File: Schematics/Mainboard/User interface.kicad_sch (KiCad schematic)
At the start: 42 parts, among them J16 OLED, J18 Power, J19 Power, J20 I0, J21 Data, J22 Data, J23 I1, J24 I2C OLED 0, J25 I2C OLED 1, J26 I2C OLED 2, J27 I2C OLED 3, J28 I2C OLED 4, J29 I2C OLED 5, J30 I2C OLED 6, J31 I2C OLED 7, J32 I2, J33 I3, J34 O0, J35 O1, J36 O2, J37 O3, J9 ICSP, U2 TCA9548APWR, U3 ATmega328-AU, Y1 16MHz YSX321SL

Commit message: Added Mainboard rev 1.0
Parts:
- removed C5, C6: 0u1, Capacitor_SMD:C_0603_1608Metric, symbol Device:C_Small
- removed J18, J19: Power, Connector_PinSocket_2.54mm:PinSocket_1x03_P2.54mm_Vertical, symbol Connector:Conn_01x03_Male
- removed J21, J22: Data, Connector_PinSocket_2.54mm:PinSocket_1x03_P2.54mm_Vertical, symbol Connector:Conn_01x03_Male
- removed J9: ICSP, Connector_PinSocket_2.54mm:PinSocket_2x03_P2.54mm_Vertical, symbol Connector_Generic:Conn_02x03_Odd_Even
- removed U3: ATmega328-AU, Package_QFP:TQFP-32_7x7mm_P0.8mm, symbol MCU_Microchip_ATmega:ATmega328-AU
- removed Y1: 16MHz YSX321SL, Crystal:Crystal_SMD_3225-4Pin_3.2x2.5mm, symbol Device:Crystal_GND24_Small
- added J44: Del in, custom:PinSocket_1x06_P2.54mm_Vertical, symbol Connector:Conn_01x06_Male
- added J45: Del out, custom:PinSocket_1x06_P2.54mm_Vertical, symbol Connector:Conn_01x06_Male
- added JP3, JP4: Jumper, Jumper:SolderJumper-2_P1.3mm_Open_Pad1.0x1.5mm, symbol Device:Jumper
- added R17, R18, R19: 47k, Resistor_SMD:R_0603_1608Metric, symbol Device:R_Small
- added SW3, SW4: Rot, Rotary_Encoder:RotaryEncoder_Alps_EC11E-Switch_Vertical_H20mm, symbol Device:Rotary_Encoder_Switch
- added U4: PCF8574TS, Package_SO:SSOP-20_4.4x6.5mm_P0.65mm, symbol Interface_Expansion:PCF8574TS
- C4: LCSC Part (none) -> C19702
- C7, C8: value 12p -> 10u; LCSC Part (none) -> C19702
- D4: footprint LED_SMD:LED_SK6805_PLCC4_2.4x2.7mm_P1.3mm -> LED_THT:LED_BL-FL7680RGB; symbol Device:LED_ABGR -> Device:LED_BRGA
- J16, J24, J25, J26, J27, J28, J29, J30, J31: footprint Connector_PinHeader_2.54mm:PinHeader_1x04_P2.54mm_Vertical_SMD_Pin1Left -> Connector_PinSocket_2.54mm:PinSocket_1x04_P2.54mm_Vertical
- R11, R13: value 1K -> 47k; LCSC Part (none) -> C25819
- R12, R14, R15: value 10K -> 10k; LCSC Part (none) -> C25804
- R16: value 10K -> 47k; LCSC Part (none) -> C25819
- R9: LCSC Part (none) -> C22810
- U2: LCSC Part (none) -> C130026
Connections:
- net 3.3V_local is gone; now on an unnamed net: D4.1 (BK)
- net ICSP RST is gone; now on net T A: R16.1
- net SUB RX is gone; now on net +3V3: R11.2
- net SUB TX is gone; now on net +3V3: R13.2
- net XTAL1 is gone; now on net GND: C7.2
- net XTAL2 is gone; now on net +3V3: C8.1
- net +3V3: now also C7.1, D4.4 (A), J44.2 (Pin_2), R17.2, R18.2, R19.2, U4.5 (VDD)
- net ALT SCL: now also U4.2 (SCL)
- net ALT SDA: now also U4.4 (SDA)
- net GND: now also J44.5 (Pin_5), SW3.C, SW3.S2, SW4.C, SW4.S2, U4.15 (VSS), U4.6 (A0), U4.7 (A1), U4.9 (A2); no longer C7.1
- net MUX SCL: now also J44.4 (Pin_4), JP4.1; no longer R12.1, U2.22 (SCL)
- net MUX SDA: now also J44.3 (Pin_3), JP3.1; no longer R14.1, U2.23 (SDA)
- net Q A: now also R17.1, SW4.A
- net Q B: now also R13.1, SW4.B
- net Q SW: now also R19.1, SW4.S1
- net T A: now also SW3.A
- net T B: now also R11.1, SW3.B
- net T SW: now also R18.1, SW3.S1
- net at J36.1 (Pin_1): now also U4.19 (P6)
- net at J33.1 (Pin_1): now also U4.16 (P4)
- net at J23.1 (Pin_1): now also U4.12 (P2)
- net at R8.1: no longer D4.2 (BK)
- net at J37.1 (Pin_1): now also U4.20 (P7)
- net at J32.1 (Pin_1): now also U4.14 (P3)
- net at J34.1 (Pin_1): now also U4.10 (P0)
- net at J35.1 (Pin_1): now also U4.17 (P5)
- net at R10.1: now also D4.2 (RK); no longer D4.4 (RK)
- net at J20.1 (Pin_1): now also U4.11 (P1)
- new net Expand INT: U4.1 (~INT~)
- new net OLED SCL: J45.4 (Pin_4), JP4.2, R12.1, U2.22 (SCL)
- new net OLED SDA: J45.3 (Pin_3), JP3.2, R14.1, U2.23 (SDA)
- no-connect marks 3 -> 6
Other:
- note added: "I/O expander"
- note added: "OLED Deligate"
- note added: "OLED Deligate module"
- note added: "Rotary encoders"
- note removed: "CL = (C1 * C2) / (C1 + C2) + Cstray 9pF = (12pF^2)/(12pF*2) + 3pF"
- note removed: "Rot enc module"
- moved on the sheet: D4, J16, J20, J23, J32, J33, J34, J35, J36, J37, R10, R8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

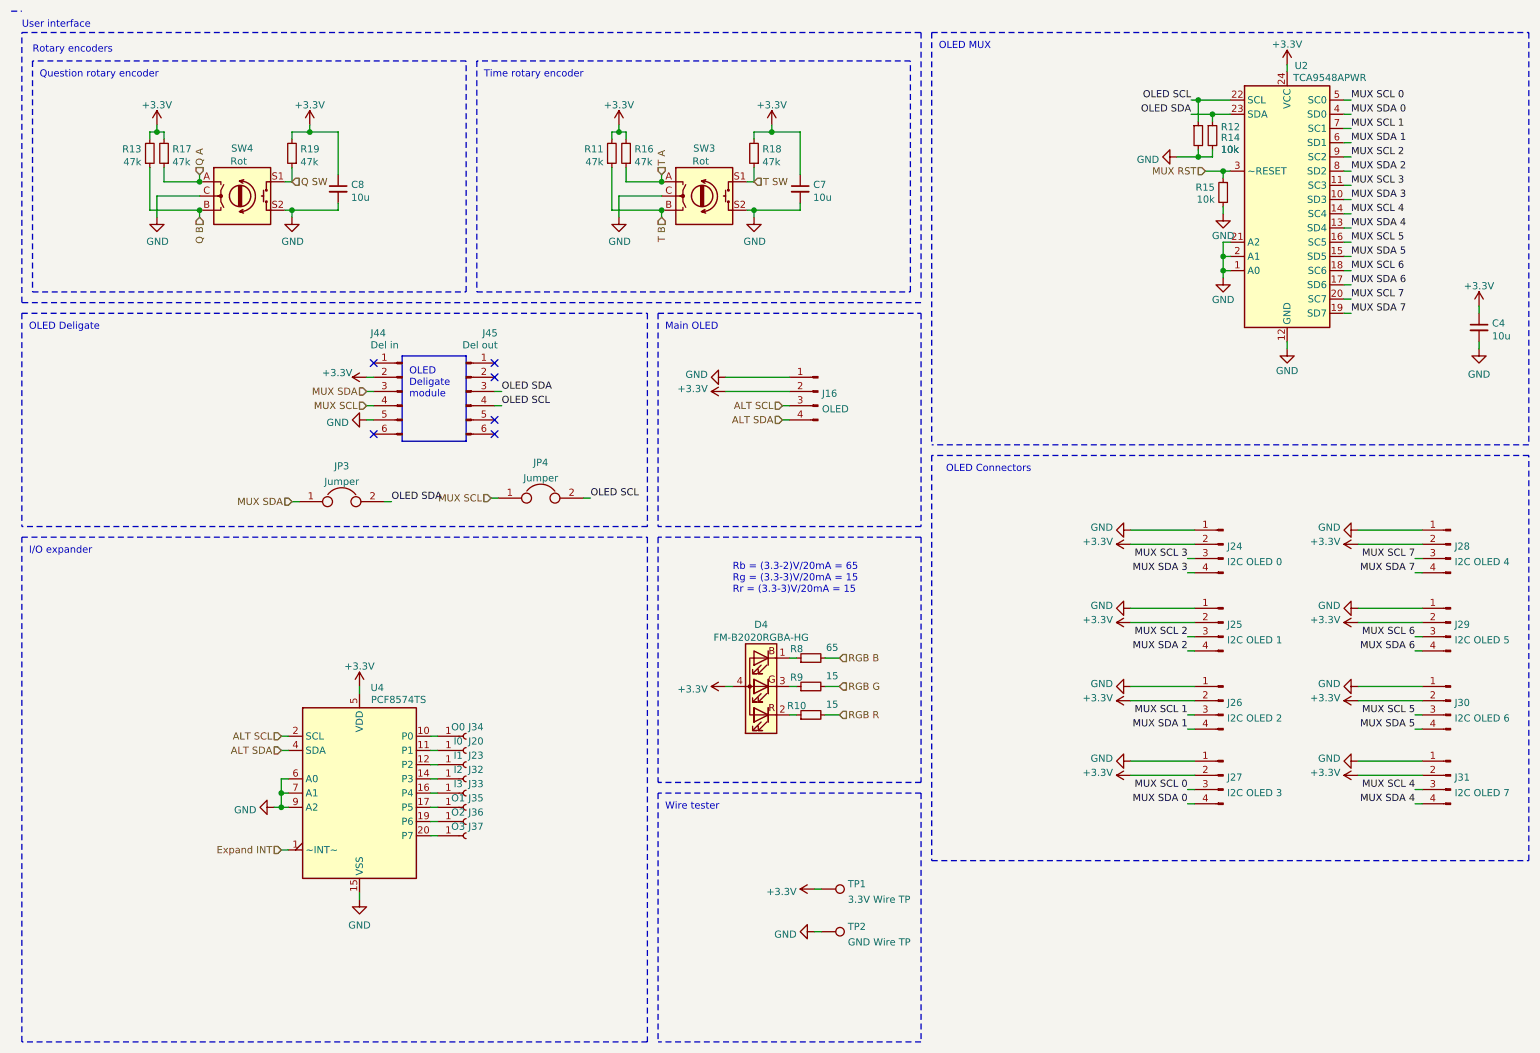
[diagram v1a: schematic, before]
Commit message: Updated I2C power
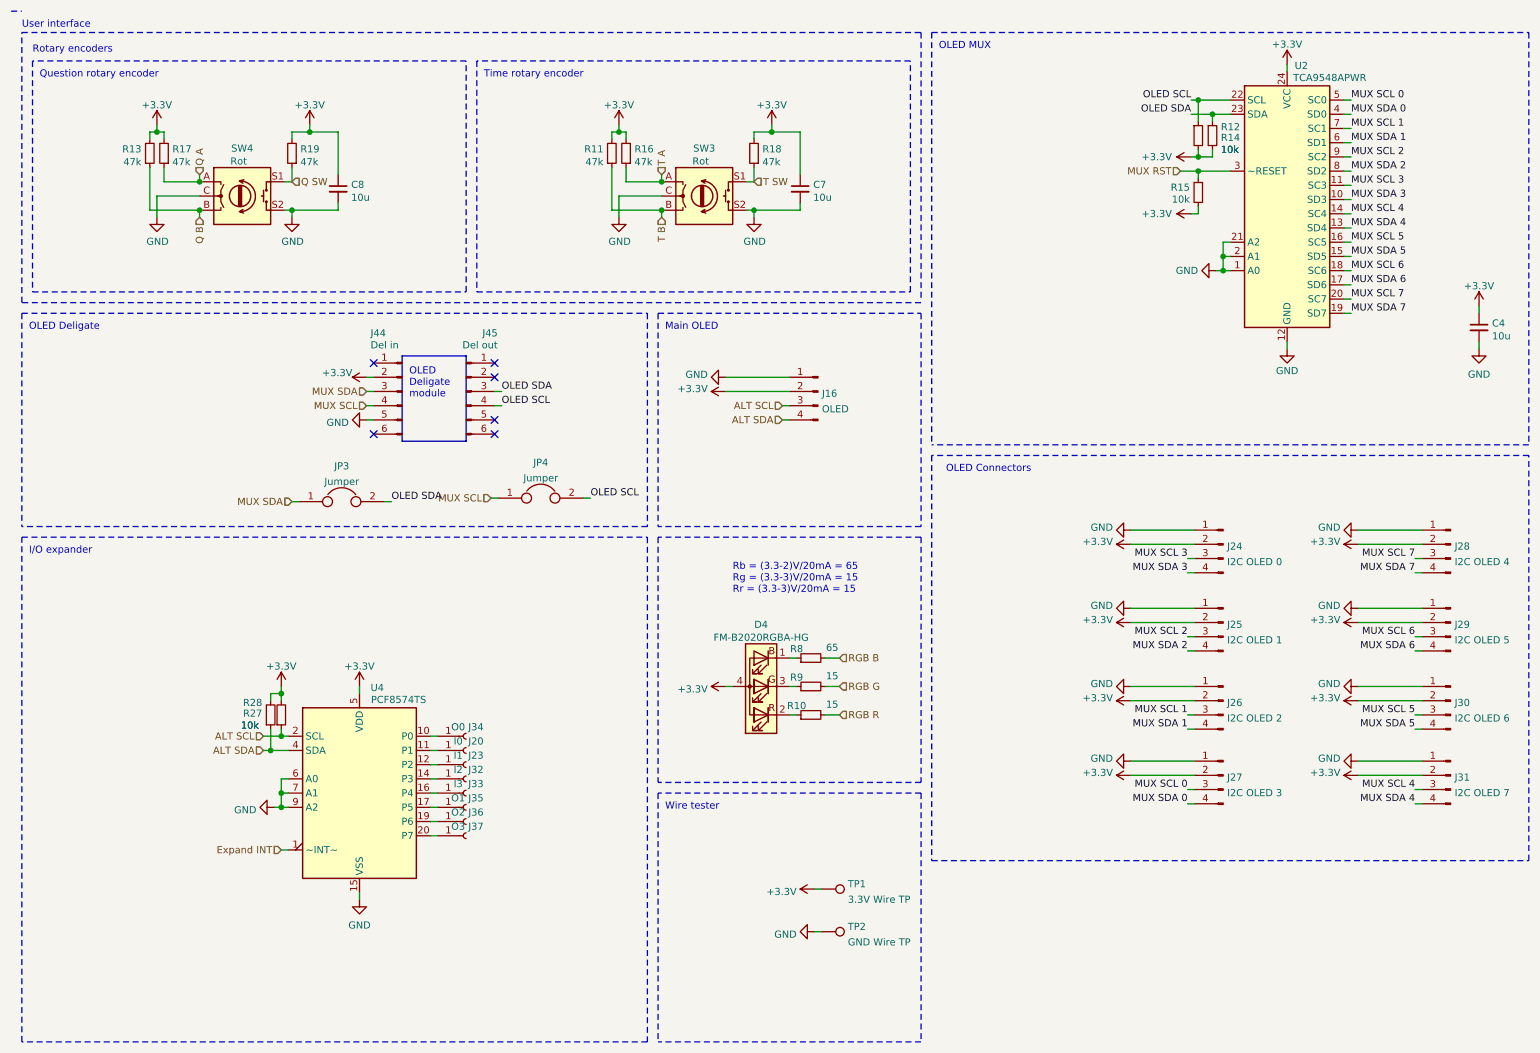
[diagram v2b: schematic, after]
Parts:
- added R27, R28: 10k, Resistor_SMD:R_0603_1608Metric, symbol Device:R_Small
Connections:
- net +3V3: now also R12.2, R14.2, R15.2, R27.2, R28.2
- net ALT SCL: now also R28.1
- net ALT SDA: now also R27.1
- net GND: no longer R12.2, R14.2, R15.2
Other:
- moved on the sheet: R15

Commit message: Final print version mainboard
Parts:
- C7, C8: value 10u -> 1u; LCSC Part C19702 -> C15849
- R18, R19: value 47k -> 10k; LCSC Part C25819 -> C25804
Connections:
- net +3V3: no longer C7.1, C8.1
- net Q SW: now also C8.1
- net T SW: now also C7.1
- net Expand INT: no longer names the net of U4.1 (~INT~)
- no-connect marks 6 -> 7
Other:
- moved on the sheet: C8
